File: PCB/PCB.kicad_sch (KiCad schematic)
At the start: 29 parts, among them J1 Conn_01x14_Socket, J2 Conn_01x08_Socket, J3 Conn_01x08_Socket, J4 Conn_01x02_Socket, J5 Conn_01x08_Socket, SW1 SW_SPDT, U1 Pico, U2 Mini360

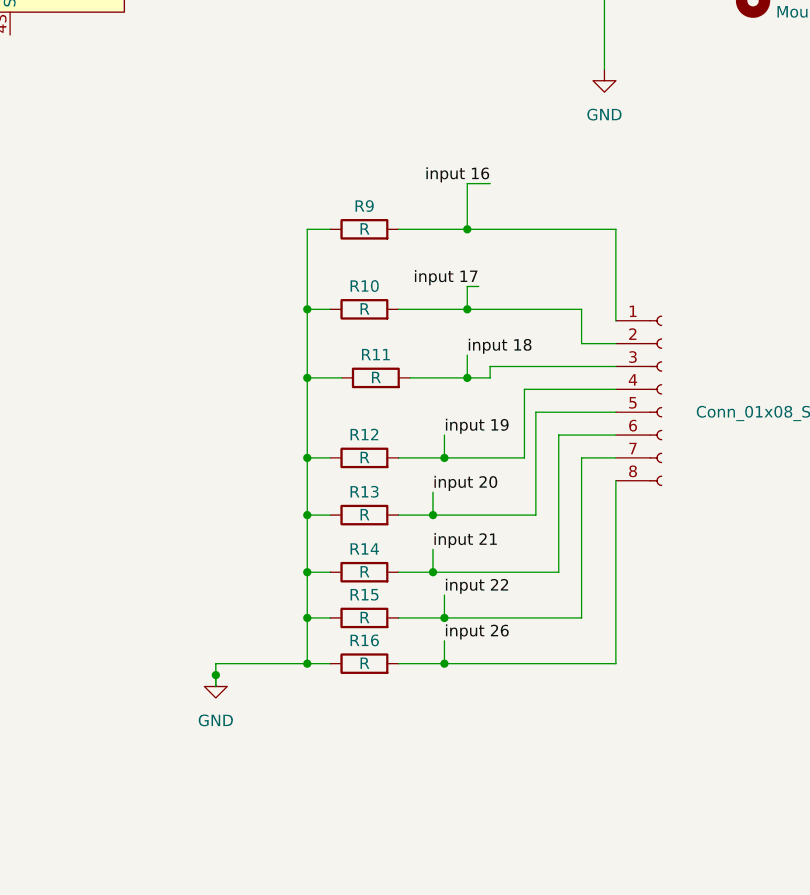
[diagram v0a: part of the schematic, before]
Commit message: updated to use internal pull down resistors, remove them from PCB design
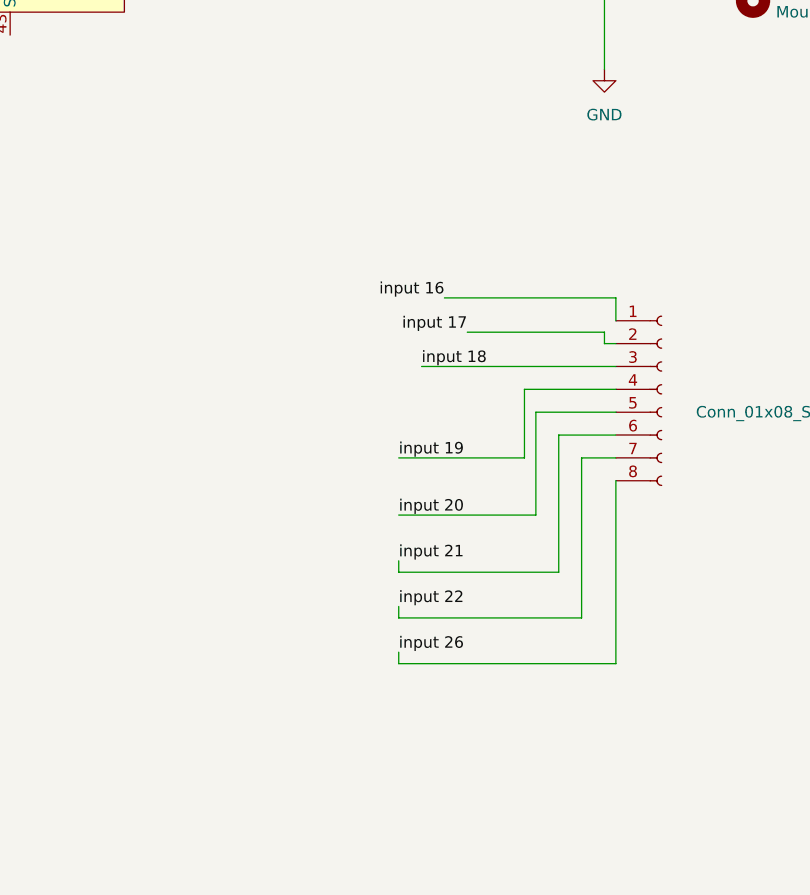
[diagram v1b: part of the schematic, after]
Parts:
- removed R10, R11, R12, R13, R14, R15, R16, R9: R, Resistor_SMD:R_0805_2012Metric, symbol Device:R

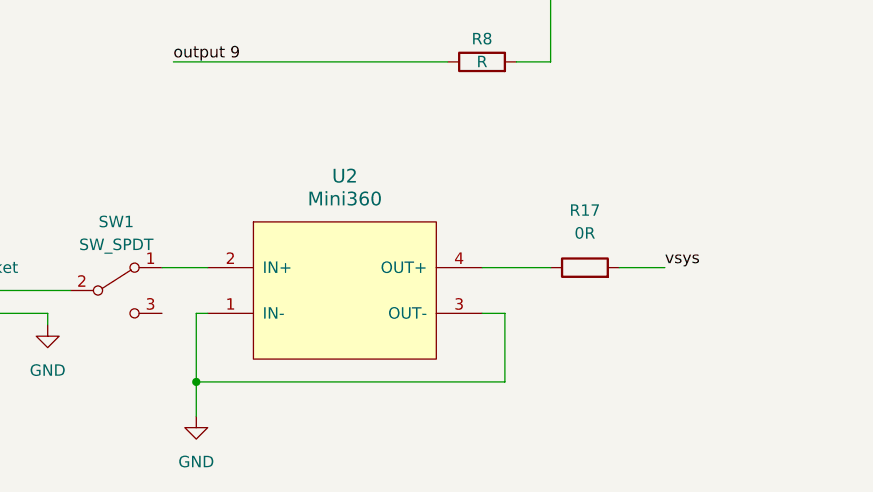
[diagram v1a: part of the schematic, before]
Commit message: 3D model changes, added ETH passthrough and remodelled AA battery bracket
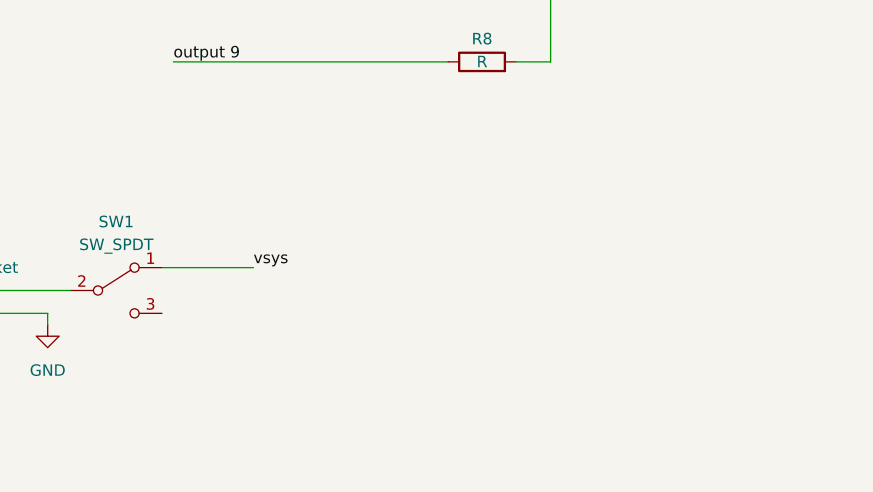
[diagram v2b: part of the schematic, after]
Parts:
- removed R17: 0R, Jumper:SolderJumper-2_P1.3mm_Open_Pad1.0x1.5mm, symbol Device:R
- removed U2: Mini360, voltage reg:Mini360_step-down, symbol PiPico:Mini360
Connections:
- net vsys: now also SW1.1 (A)
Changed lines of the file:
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@@
   (junction (at 104.14 113.03) (diameter 0) (color 0 0 0 0)
   )
-  (junction (at 63.5 173.99) (diameter 0) (color 0 0 0 0)
-  )
   (junction (at 104.14 97.79) (diameter 0) (color 0 0 0 0)
   )
@@
     (stroke (width 0) (type default))
   )
-  (wire (pts (xy 110.49 161.29) (xy 115.57 161.29))
-    (stroke (width 0) (type default))
-  )
   (wire (pts (xy 88.9 102.87) (xy 88.9 107.95))
     (stroke (width 0) (type default))
@@
     (stroke (width 0) (type default))
   )
-  (wire (pts (xy 63.5 173.99) (xy 63.5 177.8))
-    (stroke (width 0) (type default))
-  )
   (wire (pts (xy 81.28 100.33) (xy 104.14 100.33))
     (stroke (width 0) (type default))
@@
     (stroke (width 0) (type default))
   )
-  (wire (pts (xy 95.25 161.29) (xy 102.87 161.29))
-    (stroke (width 0) (type default))
-  )
   (wire (pts (xy 175.26 67.31) (xy 199.39 67.31))
     (stroke (width 0) (type default))
@@
     (stroke (width 0) (type default))
   )
-  (wire (pts (xy 95.25 166.37) (xy 97.79 166.37))
-    (stroke (width 0) (type default))
-  )
   (wire (pts (xy 60.96 100.33) (xy 73.66 100.33))
     (stroke (width 0) (type default))
@@
     (stroke (width 0) (type default))
   )
-  (wire (pts (xy 59.69 161.29) (xy 64.77 161.29))
+  (wire (pts (xy 59.69 161.29) (xy 69.85 161.29))
     (stroke (width 0) (type default))
   )
@@
     (stroke (width 0) (type default))
   )
-  (wire (pts (xy 97.79 173.99) (xy 63.5 173.99))
-    (stroke (width 0) (type default))
-  )
   (wire (pts (xy 137.16 24.13) (xy 139.7 24.13))
     (stroke (width 0) (type default))
@@
     (stroke (width 0) (type default))
   )
-  (wire (pts (xy 64.77 166.37) (xy 63.5 166.37))
-    (stroke (width 0) (type default))
-  )
-  (wire (pts (xy 97.79 166.37) (xy 97.79 173.99))
-    (stroke (width 0) (type default))
-  )
   (wire (pts (xy 92.71 105.41) (xy 104.14 105.41))
     (stroke (width 0) (type default))
@@
   )
   (wire (pts (xy 125.73 67.31) (xy 125.73 46.99))
-    (stroke (width 0) (type default))
-  )
-  (wire (pts (xy 63.5 166.37) (xy 63.5 173.99))
     (stroke (width 0) (type default))
   )
@@
     (effects (font (size 1.27 1.27)) (justify right bottom))
   )
-  (label "vsys" (at 115.57 161.29 0) (fields_autoplaced)
+  (label "vsys" (at 69.85 161.29 0) (fields_autoplaced)
     (effects (font (size 1.27 1.27)) (justify left bottom))
   )
@@
         (path "/8ef2405f-6785-4ccc-a510-a317fe091b0a"
           (reference "#PWR04") (unit 1)
-        )
-      )
-    )
-  )
-  (symbol (lib_id "PiPico:Mini360") (at 80.01 163.83 0) (unit 1)
-    (in_bom yes) (on_board yes) (dnp no) (fields_autoplaced)
-    (property "Reference" "U2" (at 80.01 151.13 0)
-      (effects (font (size 1.524 1.524)))
-    )
-    (property "Value" "Mini360" (at 80.01 153.67 0)
-      (effects (font (size 1.524 1.524)))
-    )
-    (property "Footprint" "voltage reg:Mini360_step-down" (at 80.01 163.83 0)
-      (effects (font (size 1.524 1.524)) hide)
-    )
-    (property "Datasheet" "" (at 80.01 163.83 0)
-      (effects (font (size 1.524 1.524)) hide)
-    )
-    (pin "1")
-    (pin "2")
-    (pin "3")
-    (pin "4")
-    (instances
-      (project "PCB"
-        (path "/8ef2405f-6785-4ccc-a510-a317fe091b0a"
-          (reference "U2") (unit 1)
         )
       )
@@
     )
   )
-  (symbol (lib_id "Device:R") (at 106.68 161.29 90) (unit 1)
-    (in_bom yes) (on_board yes) (dnp no) (fields_autoplaced)
-    (property "Reference" "R17" (at 106.68 154.94 90)
-      (effects (font (size 1.27 1.27)))
-    )
-    (property "Value" "0R" (at 106.68 157.48 90)
-      (effects (font (size 1.27 1.27)))
-    )
-    (property "Footprint" "Jumper:SolderJumper-2_P1.3mm_Open_Pad1.0x1.5mm" (at 106.68 163.068 90)
-      (effects (font (size 1.27 1.27)) hide)
-    )
-    (property "Datasheet" "~" (at 106.68 161.29 0)
-      (effects (font (size 1.27 1.27)) hide)
-    )
-    (pin "1")
-    (pin "2")
-    (instances
-      (project "PCB"
-        (path "/8ef2405f-6785-4ccc-a510-a317fe091b0a"
-          (reference "R17") (unit 1)
-        )
-      )
-    )
-  )
   (symbol (lib_id "Connector:Conn_01x08_Socket") (at 109.22 102.87 0) (unit 1)
     (in_bom yes) (on_board yes) (dnp no) (fields_autoplaced)
@@
         )
       )
-    )
-  )
-  (symbol (lib_id "power:GND") (at 63.5 177.8 0) (unit 1)
-    (in_bom yes) (on_board yes) (dnp no) (fields_autoplaced)
-    (property "Reference" "#PWR07" (at 63.5 184.15 0)
-      (effects (font (size 1.27 1.27)) hide)
-    )
-    (property "Value" "GND" (at 63.5 182.88 0)
-      (effects (font (size 1.27 1.27)))
-    )
-    (property "Footprint" "" (at 63.5 177.8 0)
-      (effects (font (size 1.27 1.27)) hide)
-    )
-    (property "Datasheet" "" (at 63.5 177.8 0)
-      (effects (font (size 1.27 1.27)) hide)
-    )
-    (pin "1")
-    (instances
-      (project "PCB"
-        (path "/8ef2405f-6785-4ccc-a510-a317fe091b0a"
-          (reference "#PWR07") (unit 1)
-        )
-      )
